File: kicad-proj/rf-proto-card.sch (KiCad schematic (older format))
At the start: 0 parts

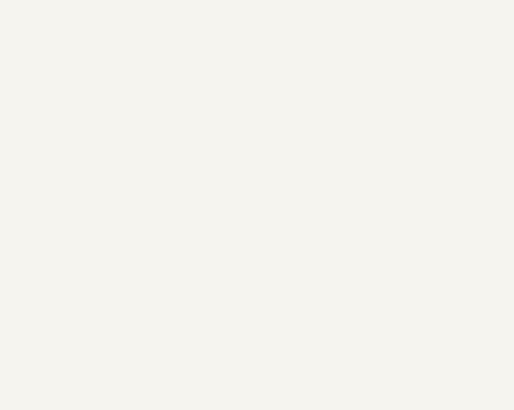
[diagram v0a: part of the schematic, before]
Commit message: Added PCB outline and screw holes
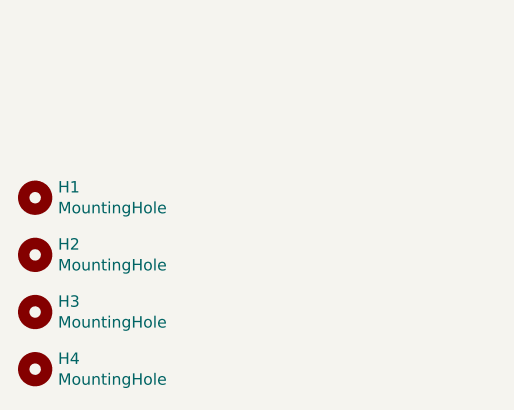
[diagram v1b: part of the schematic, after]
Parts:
- added H1, H2, H3, H4: MountingHole, MountingHole:MountingHole_2.7mm_M2.5_Pad_Via, symbol Mechanical:MountingHole
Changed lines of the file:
@@
 $EndDescr
 $Comp
-L sw-logo:LOGO #G?
+L sw-logo:LOGO #G1
 U 1 1 613B3FE6
 P 10250 6850
-F 0 "#G?" H 10250 6647 60  0001 C CNN
+F 0 "#G1" H 10250 6647 60  0001 C CNN
 F 1 "LOGO" H 10250 7053 60  0001 C CNN
 F 2 "" H 10250 6850 50  0001 C CNN
@@
 $EndComp
 $Comp
-L Graphic:Logo_Open_Hardware_Small #LOGO?
+L Graphic:Logo_Open_Hardware_Small #LOGO1
 U 1 1 613B6B5C
 P 10850 850
-F 0 "#LOGO?" H 10850 1125 50  0001 C CNN
+F 0 "#LOGO1" H 10850 1125 50  0001 C CNN
 F 1 "Logo_Open_Hardware_Small" H 10850 625 50  0001 C CNN
 F 2 "" H 10850 850 50  0001 C CNN
@@
 Text Notes 10550 1150 0    50   ~ 0
 Open Hardware
+$Comp
+L Mechanical:MountingHole H1
+U 1 1 613B48A3
+P 6150 6750
+F 0 "H1" H 6250 6796 50  0000 L CNN
+F 1 "MountingHole" H 6250 6705 50  0000 L CNN
+F 2 "MountingHole:MountingHole_2.7mm_M2.5_Pad_Via" H 6150 6750 50  0001 C CNN
+F 3 "~" H 6150 6750 50  0001 C CNN
+	1    6150 6750
+	1    0    0    -1
+$EndComp
+$Comp
+L Mechanical:MountingHole H2
+U 1 1 613B57D5
+P 6150 7000
+F 0 "H2" H 6250 7046 50  0000 L CNN
+F 1 "MountingHole" H 6250 6955 50  0000 L CNN
+F 2 "MountingHole:MountingHole_2.7mm_M2.5_Pad_Via" H 6150 7000 50  0001 C CNN
+F 3 "~" H 6150 7000 50  0001 C CNN
+	1    6150 7000
+	1    0    0    -1
+$EndComp
+$Comp
+L Mechanical:MountingHole H3
+U 1 1 613B5B73
+P 6150 7250
+F 0 "H3" H 6250 7296 50  0000 L CNN
+F 1 "MountingHole" H 6250 7205 50  0000 L CNN
+F 2 "MountingHole:MountingHole_2.7mm_M2.5_Pad_Via" H 6150 7250 50  0001 C CNN
+F 3 "~" H 6150 7250 50  0001 C CNN
+	1    6150 7250
+	1    0    0    -1
+$EndComp
+$Comp
+L Mechanical:MountingHole H4
+U 1 1 613B5D7B
+P 6150 7500
+F 0 "H4" H 6250 7546 50  0000 L CNN
+F 1 "MountingHole" H 6250 7455 50  0000 L CNN
+F 2 "MountingHole:MountingHole_2.7mm_M2.5_Pad_Via" H 6150 7500 50  0001 C CNN
+F 3 "~" H 6150 7500 50  0001 C CNN
+	1    6150 7500
+	1    0    0    -1
+$EndComp
 $EndSCHEMATC

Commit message: layout done
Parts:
- added A1, A10, A11, A12, A13, A14, A2, A3, A4, A5, A6, A7, A8, A9, B1, B10, B11, B12, B13, B14, B2, B3, B4, B5, B6, B7, B8, B9: R, Resistor_SMD:R_0603_1608Metric, symbol Device:R
- added J1: sma-a-in, Connector_Coaxial:SMA_Amphenol_132134-10_Vertical, symbol Connector:Conn_Coaxial
- added J2: sma-b-in, Connector_Coaxial:SMA_Amphenol_132134-10_Vertical, symbol Connector:Conn_Coaxial
- added J3: sma-a-out, Connector_Coaxial:SMA_Amphenol_132134-10_Vertical, symbol Connector:Conn_Coaxial
- added J4: sma-b-out, Connector_Coaxial:SMA_Amphenol_132134-10_Vertical, symbol Connector:Conn_Coaxial
- added J5, J6: RF_Shield_One_Piece, RF_Shielding:Laird_Technologies_BMI-S-209-F_29.36x18.50mm, symbol Device:RF_Shield_One_Piece
- added TP1: rail-a-in, TestPoint:TestPoint_Pad_D1.0mm, symbol Connector:TestPoint
- added TP2, TP4, TP6, TP8: gnd, TestPoint:TestPoint_Pad_D1.0mm, symbol Connector:TestPoint
- added TP3: rail-b-in, TestPoint:TestPoint_Pad_D1.0mm, symbol Connector:TestPoint
- added TP5: rail-a-out, TestPoint:TestPoint_Pad_D1.0mm, symbol Connector:TestPoint
- added TP7: rail-b-out, TestPoint:TestPoint_Pad_D1.0mm, symbol Connector:TestPoint
- added U1, U2: GALI-52, Package_TO_SOT_SMD:SOT-89-3, symbol RF_Amplifier:GALI-52
- added Z1, Z2, Z3, Z4: proto-area, rf-proto-card:proto-area, symbol rf-proto-card:proto-area
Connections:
- new net: A3.1, A5.2, J1.1 (In)
- new net: A5.1, A7.1, U1.1
- new net: A1.1, A2.1, A3.2, A4.2
- new net: A4.1, A6.1, A7.2
- new net: A1.2, TP1.1
- new net: A11.1, A13.1, J3.1 (In)
- new net: A11.2, A9.1, U1.3
- new net: A10.2, A8.1, A9.2
- new net: A10.1, A12.1, A13.2, A14.1
- new net: A14.2, TP5.1
- new net: B3.1, B5.1, J2.1 (In)
- new net: B1.1, B2.1, B3.2, B4.1
- new net: B1.2, TP3.1
- new net: B5.2, B7.1, U2.1
- new net: B11.1, B9.1, U2.3
- new net: B11.2, B13.1, J4.1 (In)
- new net: B4.2, B6.1, B7.2
- new net: B10.1, B8.1, B9.2
- new net: B10.2, B12.1, B13.2, B14.1
- new net: B14.2, TP7.1
- new net GND: A12.2, A2.2, A6.2, A8.2, B12.2, B2.2, B6.2, B8.2, J1.2 (Ext), J2.2 (Ext), J3.2 (Ext), J4.2 (Ext), J5.1 (Shield), J6.1 (Shield), TP2.1, TP4.1, TP6.1, TP8.1, U1.2 (GND), U2.2 (GND)
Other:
- note added: "Impedence calculations:\n\nPCB specs:\n- PCB layers = 2\n- Er = 4.29\n- Copper thickness = 1oz (35um)\n- PCB thickness = 0.8mm (0.7 - 0.75 core)\n\nTransmission line specs:\n- Line impedence = 50 ohm\n- Topology: co-planer waveguide with ground layer\n- Trace width = 0.95mm (for 0603)\n- Gap = 0.26mm"

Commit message: Complete and gerber exported
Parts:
- added FID1: card-info-gold, rf-proto-card:front-info-gold, symbol Mechanical:Fiducial
- added FID2: card-info-white, rf-proto-card:front-info-white, symbol Mechanical:Fiducial
- J2: renamed from J1; value sma-a-in -> sma-a
- J3: value sma-a-out -> sma-b
- J5: renamed from J2; value sma-b-in -> sma-c
- J6: renamed from J4; value sma-b-out -> sma-d
- TP1: value rail-a-in -> vbias-a
- TP2: renamed from TP5; value rail-a-out -> vbias-b
- TP5: renamed from TP3; value rail-b-in -> vbias-c
- TP6: renamed from TP7; value rail-b-out -> vbias-d
- renumbered A6 to A3, A3 to A5, A7 to A6, A5 to A7, A8 to B1, A12 to B2, A14 to B3, A10 to B4, A9 to B5, A13 to B6, A11 to B7, B1 to C1, B2 to C2, B6 to C3, B4 to C4, B3 to C5, B7 to C6, B5 to C7, B8 to D1, B12 to D2, B14 to D3, B10 to D4, B9 to D5, B13 to D6, B11 to D7, J5 to J1, J6 to J4, TP2 to TP3, TP6 to TP4, TP4 to TP7
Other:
- moved on the sheet: A1, A2, A3, A4, A5, A6, A7, B1, B2, B3, B4, B5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

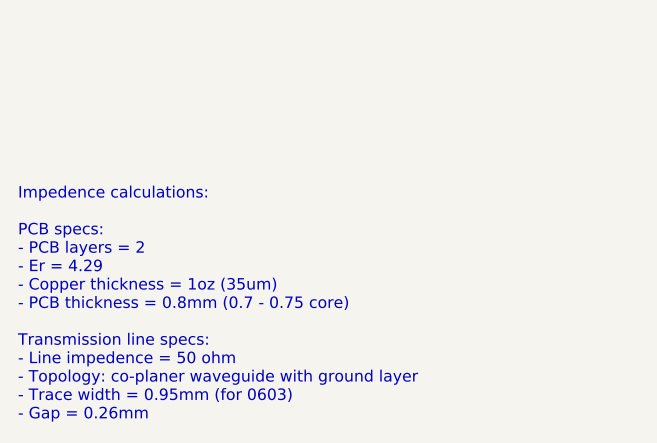
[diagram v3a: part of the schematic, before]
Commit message: Updated PCB to correct board core thickness of 0.711mm
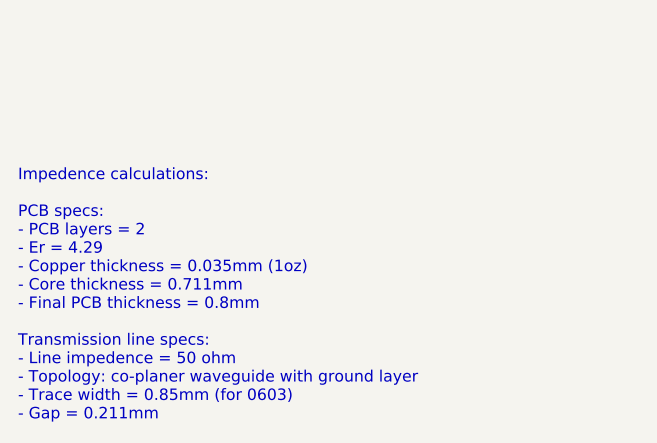
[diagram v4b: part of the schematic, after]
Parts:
- U1, U2: footprint Package_TO_SOT_SMD:SOT-89-3 -> rf-proto-card:SOT-89-3
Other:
- note added: "Impedence calculations:\n\nPCB specs:\n- PCB layers = 2\n- Er = 4.29\n- Copper thickness = 0.035mm (1oz)\n- Core thickness = 0.711mm\n- Final PCB thickness = 0.8mm\n\nTransmission line specs:\n- Line impedence = 50 ohm\n- Topology: co-planer waveguide with ground layer\n- Trace width = 0.85mm (for 0603)\n- Gap = 0.211mm"
- note removed: "Impedence calculations:\n\nPCB specs:\n- PCB layers = 2\n- Er = 4.29\n- Copper thickness = 1oz (35um)\n- PCB thickness = 0.8mm (0.7 - 0.75 core)\n\nTransmission line specs:\n- Line impedence = 50 ohm\n- Topology: co-planer waveguide with ground layer\n- Trace width = 0.95mm (for 0603)\n- Gap = 0.26mm"
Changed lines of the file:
@@
 Sheet 1 1
 Title "RF Proto Business Card"
-Date "2021-09-14"
-Rev "1"
+Date "2021-09-19"
+Rev "2"
 Comp "Silicon Witchery AB"
 Comment1 "Engineer: Raj Nakarja"
@@
 F 0 "U1" H 4450 3625 50  0000 C CNN
 F 1 "GALI-52" H 4450 3626 50  0001 C CNN
-F 2 "Package_TO_SOT_SMD:SOT-89-3" H 4500 3750 50  0001 C CNN
+F 2 "rf-proto-card:SOT-89-3" H 4500 3750 50  0001 C CNN
 F 3 "https://www.minicircuits.com/pdfs/GALI-52+.pdf" H 4450 3350 50  0001 C CNN
 	1    4450 3350
@@
 $EndComp
 Text Notes 800  7450 0    50   ~ 0
-Impedence calculations:\n\nPCB specs:\n- PCB layers = 2\n- Er = 4.29\n- Copper thickness = 1oz (35um)\n- PCB thickness = 0.8mm (0.7 - 0.75 core)\n\nTransmission line specs:\n- Line impedence = 50 ohm\n- Topology: co-planer waveguide with ground layer\n- Trace width = 0.95mm (for 0603)\n- Gap = 0.26mm
+Impedence calculations:\n\nPCB specs:\n- PCB layers = 2\n- Er = 4.29\n- Copper thickness = 0.035mm (1oz)\n- Core thickness = 0.711mm\n- Final PCB thickness = 0.8mm\n\nTransmission line specs:\n- Line impedence = 50 ohm\n- Topology: co-planer waveguide with ground layer\n- Trace width = 0.85mm (for 0603)\n- Gap = 0.211mm
 $Comp
 L power:GND #PWR018
@@
 F 0 "U2" H 4450 5525 50  0000 C CNN
 F 1 "GALI-52" H 4450 5526 50  0001 C CNN
-F 2 "Package_TO_SOT_SMD:SOT-89-3" H 4500 5650 50  0001 C CNN
+F 2 "rf-proto-card:SOT-89-3" H 4500 5650 50  0001 C CNN
 F 3 "https://www.minicircuits.com/pdfs/GALI-52+.pdf" H 4450 5250 50  0001 C CNN
 	1    4450 5250
